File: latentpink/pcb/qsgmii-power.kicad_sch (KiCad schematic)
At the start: 89 parts, among them U1 VSC8512

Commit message: Continued work on QSGMII subsystem
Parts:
- added C262, C263, C265, C283, C284: 22 uF, symbol device:C
- added C264, C266, C268, C269, C270, C271, C272, C273, C274, C275, C276, C277, C278, C279, C280, C281, C282, C285, C286, C287, C288, C290, C291, C294, C295, C296, C297, C298, C299, C300, C302, C303, C304, C305, C307, C308, C309, C310, C312, C313, C314, C315, C316, C317, C318, C319, C320, C321, C322, C323, C324, C325, C326, C327, C328, C329, C330, C331, C332, C333: 0.47 uF, azonenberg_pcb:EIA_0402_CAP_NOSILK, symbol device:C
- added C267, C292, C293, C306, C311: 4.7 uF, azonenberg_pcb:EIA_0603_CAP_NOSILK, symbol device:C
- added C289, C301: 47 uF, symbol device:C
- added L2, L3, L4, L5: HI1206N101R-10, azonenberg_pcb:EIA_1206_CAP_NOSILK, symbol passive-azonenberg:INDUCTOR_PWROUT
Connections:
- net 1V0: now also C262.1, C263.1, C284.1, L2.2, L3.2, L5.2
- net 2V5: now also C283.1, C301.1, C302.1, C303.1, C306.1, C307.1, C308.1, C311.1, C312.1, C313.1, C316.1, C317.1, C318.1, C321.1, C322.1, C323.1, C324.1, C325.1, C328.1, C329.1, C330.1, C331.1, C332.1, C333.1, L4.2
- net A1V0_VSC: now also C264.1, C265.1, C266.1, C267.1, C268.1, C269.1, C270.1, C271.1, C272.1, C273.1, C274.1, C275.1, C276.1, C277.1, C278.1, C279.1, C280.1, C281.1, C282.1, C285.1, C286.1, C287.1, C288.1, C290.1, C291.1, C294.1, L3.1
- net A1V0_VSC_SERDES1: now also L2.1
- net A1V0_VSC_SERDES2: now also U1.AD19 (VDD_VS), U1.AD20 (VDD_VS), U1.AD21 (VDD_VS), C289.1, C292.1, C293.1, C295.1, C296.1, C297.1, C298.1, C299.1, C300.1, C304.1, C305.1, C309.1, C310.1, C314.1, C315.1, C319.1, C320.1, C326.1, C327.1, L5.1
- net A2V5_VSC: now also L4.1
- net GND: now also C262.2, C263.2, C264.2, C265.2, C266.2, C267.2, C268.2, C269.2, C270.2, C271.2, C272.2, C273.2, C274.2, C275.2, C276.2, C277.2, C278.2, C279.2, C280.2, C281.2, C282.2, C283.2, C284.2, C285.2, C286.2, C287.2, C288.2, C289.2, C290.2, C291.2, C292.2, C293.2, C294.2, C295.2, C296.2, C297.2, C298.2, C299.2, C300.2, C301.2, C302.2, C303.2, C304.2, C305.2, C306.2, C307.2, C308.2, C309.2, C310.2, C311.2, C312.2, C313.2, C314.2, C315.2, C316.2, C317.2, C318.2, C319.2, C320.2, C321.2, C322.2, C323.2, C324.2, C325.2, C326.2, C327.2, C328.2, C329.2, C330.2, C331.2, C332.2, C333.2
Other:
- note added: "Ferrites 80-100 ohms @ 100 MHz Vendor recommends: Panasonic EXCELSA39 (thru hole) Steward HI1206N101R-00 (EOL)"
- note added: "VDD_AH decoupling"
- note added: "VDD_AL decoupling"
- note added: "VDD_VS decoupling"
- note removed: "Ferrites 80-100 ohms @ 100 MHz Panasonic EXCELSA39 Steward HI1206N101R-00"
- moved on the sheet: C1, C10, C11, C12, C13, C14, C15, C16, C17, C18, C19, C2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

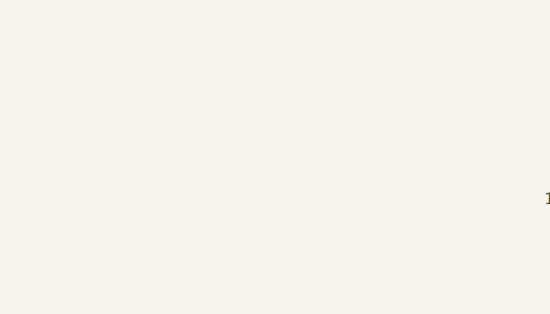
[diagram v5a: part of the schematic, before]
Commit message: Continued footprint assignment and miscellaneous missing tidbits of schematic
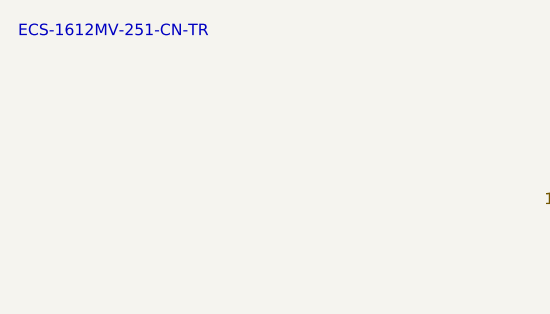
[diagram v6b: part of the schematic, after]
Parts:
- C1, C289, C301, C67: footprint (none) -> azonenberg_pcb:EIA_1210_CAP_NOSILK
- C6: footprint (none) -> azonenberg_pcb:EIA_1206_CAP_NOSILK
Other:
- note added: "ECS-1612MV-251-CN-TR"
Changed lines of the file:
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@@
   (paper "A3")
   (title_block
-    (date "2023-05-16")
+    (date "2023-05-20")
     (rev "0.1")
     (company "Antikernel Labs")
@@
     (effects (font (size 1.27 1.27)) (justify left bottom))
   )
+  (text "ECS-1612MV-251-CN-TR" (at 0 2.54 0)
+    (effects (font (size 1.27 1.27)) (justify left bottom))
+  )
   (label "1V0" (at 180.34 209.55 180)
     (effects (font (size 1.27 1.27)) (justify right bottom))
@@
       (effects (font (size 1.27 1.27)) (justify left))
     )
-    (property "Footprint" "" (id 2) (at 205.4352 217.17 0)
+    (property "Footprint" "azonenberg_pcb:EIA_1210_CAP_NOSILK" (id 2) (at 205.4352 217.17 0)
       (effects (font (size 1.27 1.27)) hide)
     )
@@
       (effects (font (size 1.27 1.27)) (justify left))
     )
-    (property "Footprint" "" (id 2) (at 56.8452 231.14 0)
+    (property "Footprint" "azonenberg_pcb:EIA_1206_CAP_NOSILK" (id 2) (at 56.8452 231.14 0)
       (effects (font (size 1.27 1.27)) hide)
     )
@@
       (effects (font (size 1.27 1.27)) (justify left))
     )
-    (property "Footprint" "" (id 2) (at 26.3652 166.37 0)
+    (property "Footprint" "azonenberg_pcb:EIA_1210_CAP_NOSILK" (id 2) (at 26.3652 166.37 0)
       (effects (font (size 1.27 1.27)) hide)
     )
@@
       (effects (font (size 1.27 1.27)) (justify left))
     )
-    (property "Footprint" "" (id 2) (at 274.0152 118.11 0)
+    (property "Footprint" "azonenberg_pcb:EIA_1210_CAP_NOSILK" (id 2) (at 274.0152 118.11 0)
       (effects (font (size 1.27 1.27)) hide)
     )
@@
       (effects (font (size 1.27 1.27)) (justify left))
     )
-    (property "Footprint" "" (id 2) (at 219.4052 179.07 0)
+    (property "Footprint" "azonenberg_pcb:EIA_1210_CAP_NOSILK" (id 2) (at 219.4052 179.07 0)
       (effects (font (size 1.27 1.27)) hide)
     )

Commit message: Finished initial schematic, ready for design review
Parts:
- C262, C263, C265, C284: footprint (none) -> azonenberg_pcb:EIA_0805_CAP_NOSILK
- C283: footprint (none) -> azonenberg_pcb:EIA_1206_CAP_NOSILK
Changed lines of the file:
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@@
       (effects (font (size 1.27 1.27)) (justify left))
     )
-    (property "Footprint" "" (id 2) (at 32.7152 257.81 0)
+    (property "Footprint" "azonenberg_pcb:EIA_0805_CAP_NOSILK" (id 2) (at 32.7152 257.81 0)
       (effects (font (size 1.27 1.27)) hide)
     )
@@
       (effects (font (size 1.27 1.27)) (justify left))
     )
-    (property "Footprint" "" (id 2) (at 181.3052 179.07 0)
+    (property "Footprint" "azonenberg_pcb:EIA_1206_CAP_NOSILK" (id 2) (at 181.3052 179.07 0)
       (effects (font (size 1.27 1.27)) hide)
     )
@@
       (effects (font (size 1.27 1.27)) (justify left))
     )
-    (property "Footprint" "" (id 2) (at 181.3052 217.17 0)
+    (property "Footprint" "azonenberg_pcb:EIA_0805_CAP_NOSILK" (id 2) (at 181.3052 217.17 0)
       (effects (font (size 1.27 1.27)) hide)
     )
@@
       (effects (font (size 1.27 1.27)) (justify left))
     )
-    (property "Footprint" "" (id 2) (at 32.7152 231.14 0)
+    (property "Footprint" "azonenberg_pcb:EIA_0805_CAP_NOSILK" (id 2) (at 32.7152 231.14 0)
       (effects (font (size 1.27 1.27)) hide)
     )
@@
       (effects (font (size 1.27 1.27)) (justify left))
     )
-    (property "Footprint" "" (id 2) (at 54.3052 257.81 0)
+    (property "Footprint" "azonenberg_pcb:EIA_0805_CAP_NOSILK" (id 2) (at 54.3052 257.81 0)
       (effects (font (size 1.27 1.27)) hide)
     )

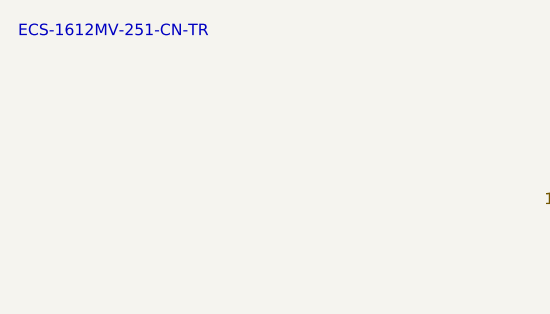
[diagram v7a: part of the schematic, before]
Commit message: Continued work on signoff review, added some more test points and SFP+ activity LEDs
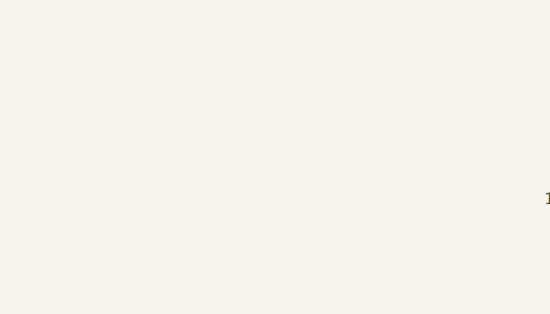
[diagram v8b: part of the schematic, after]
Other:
- note removed: "ECS-1612MV-251-CN-TR"
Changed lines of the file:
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@@
   (paper "A3")
   (title_block
-    (date "2023-05-20")
+    (date "2023-05-21")
     (rev "0.1")
     (company "Antikernel Labs")
@@
     (effects (font (size 1.27 1.27)) (justify left bottom))
   )
-  (text "ECS-1612MV-251-CN-TR" (at 0 2.54 0)
-    (effects (font (size 1.27 1.27)) (justify left bottom))
-  )
